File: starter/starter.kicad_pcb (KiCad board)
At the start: 2 copper layers, 88.3 x 97.8 mm, 44 parts, among them J1 Conn_01x04_MountingPin, J2 Conn_01x02, J3 Conn_01x04_MountingPin, J4 Conn_01x04_MountingPin, J5 Conn_01x02_MountingPin, Q1 Q_NMOS_GDS, SW1 SW_Coded_SH-7050, SW2 SW_Coded_SH-7050, U1 MCP100-475D, U2 LM1117DT-ADJ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

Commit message: Logo, fix DRC in starter
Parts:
- added G***: LOGO, shared:logo20x20, F.Cu at (77.2, 146.3)

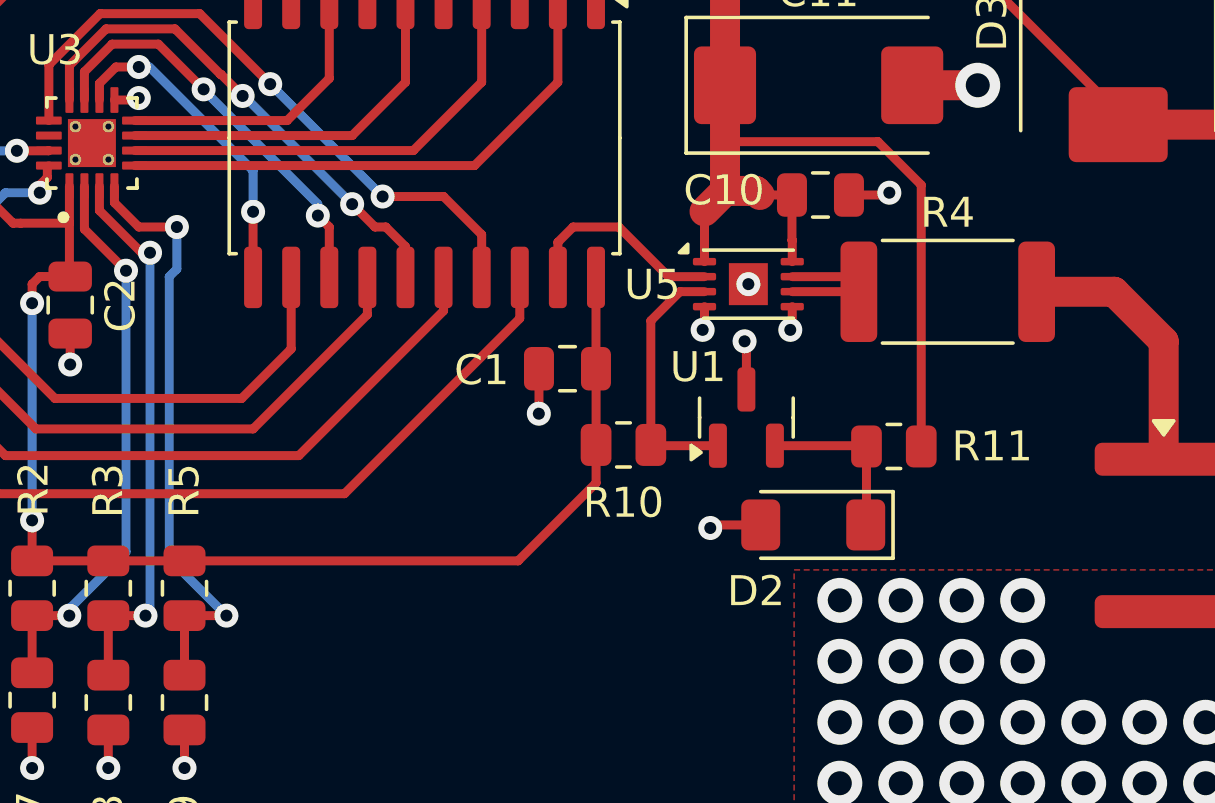
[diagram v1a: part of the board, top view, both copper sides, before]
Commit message: Fix footprint for U1 in starter board
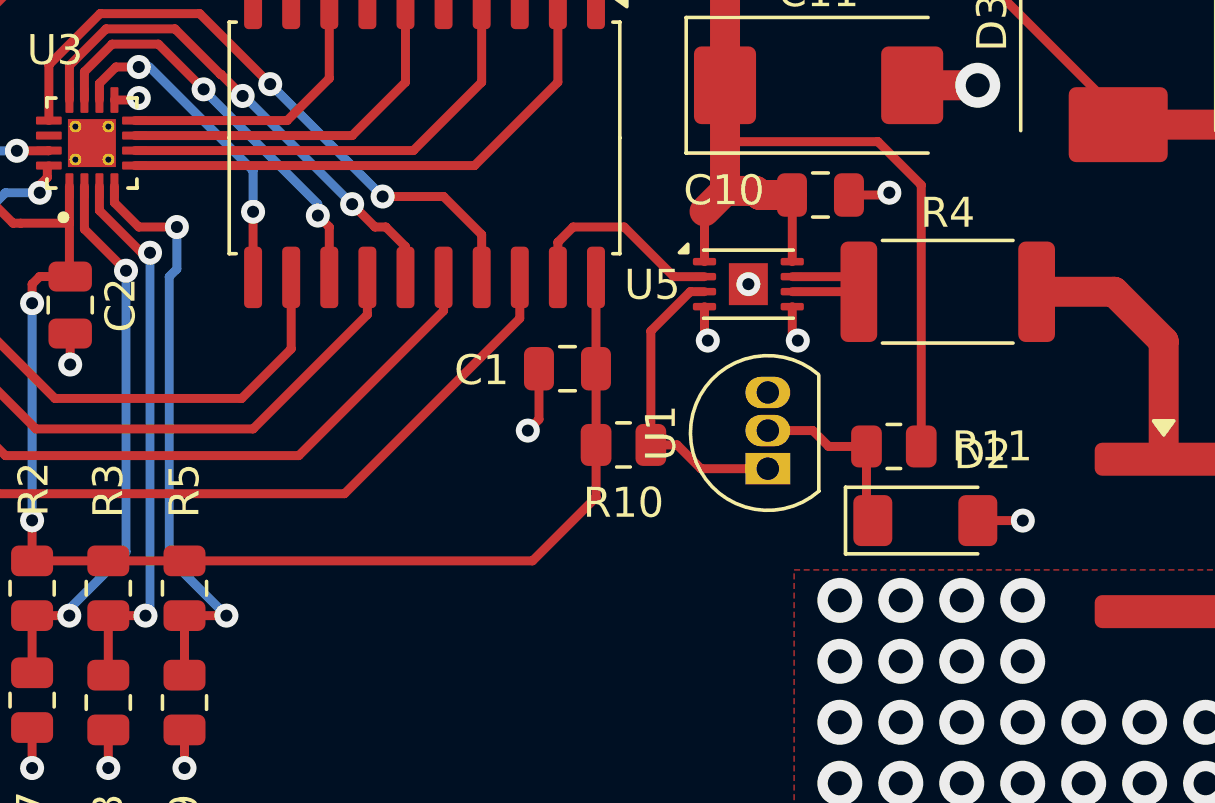
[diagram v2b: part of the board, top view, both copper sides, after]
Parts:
- U1: footprint Package_TO_SOT_SMD:SOT-23 -> Package_TO_SOT_THT:TO-92L_Inline
- moved D2 3.74 mm to (91.8, 134.5), turned to 0 degrees
- moved U1 1.85 mm to (86.5, 132.8)
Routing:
- net Net-(U1-~{RST}): track 8.58 -> 10.4 mm
- net +12V: track 91.7 -> 90.4 mm
- net GND: track 99.5 -> 99.2 mm, vias 47 -> 46

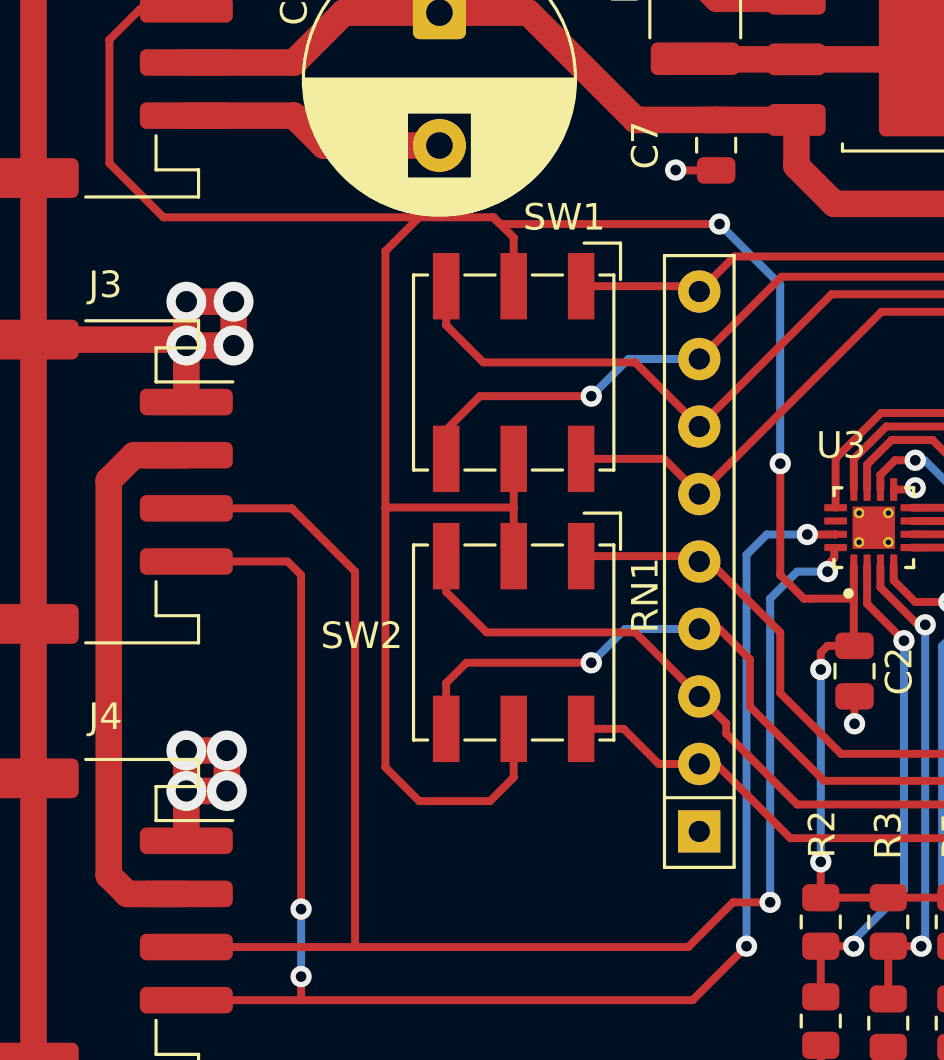
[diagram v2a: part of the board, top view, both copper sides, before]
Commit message: Fix footprint for hex encoder
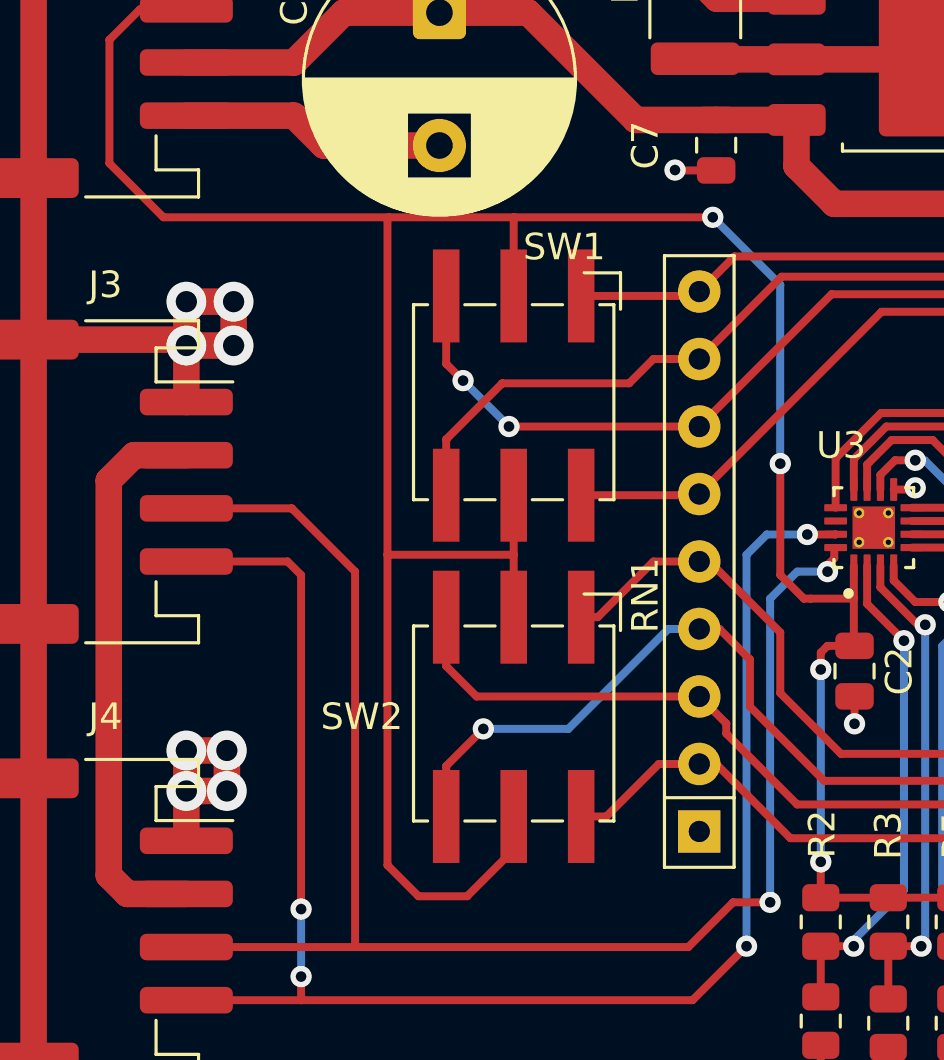
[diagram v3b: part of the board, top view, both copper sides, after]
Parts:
- moved SW2 3.05 mm to (50.4, 129.3)
- moved SW1 1.12 mm to (50.4, 117.2)
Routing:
- net +3.3V: track 130.0 -> 133.8 mm
- net Net-(RN1-R3): track 34.1 -> 35.5 mm
- net Net-(RN1-R7): track 34.5 -> 35.6 mm, vias 1 -> 0
- net Net-(RN1-R4): track 25.1 -> 25.9 mm
- net Net-(RN1-R2): track 35.8 -> 35.1 mm
- net Net-(RN1-R5): track 23.7 -> 23.2 mm
- net Net-(RN1-R6): track 33.1 -> 33.6 mm, vias 0 -> 2
